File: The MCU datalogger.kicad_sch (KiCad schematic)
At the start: 0 parts

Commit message: Initial commit before syncing with GitHub
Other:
- company: (none) -> Precious Nedilyn B. Echapare
- title: (none) -> MCU Datalogger
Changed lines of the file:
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@@
 	(generator_version "9.0")
 	(paper "A4")
+	(title_block
+		(title "MCU Datalogger")
+		(rev "1")
+		(company "Precious Nedilyn B. Echapare")
+	)
 	(sheet_instances
 		(path "/"

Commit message: Have added required symbols to the schematic sheets.
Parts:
- added BT1: Battery, symbol Device:Battery
- added C1, C2, C3, C4: C, symbol Device:C
- added C5: C_Polarized, symbol Device:C_Polarized
- added D1, D2: LED, symbol Device:LED
- added R1, R2, R3, R4, R5, R6, R7: R, symbol Device:R
- added U1: ATMEGA328P-AU, ATMEGA328P-AU:QFP80P900X900X120-32N, symbol ATMEGA328P_AU:ATMEGA328P-AU
- added U2: DS1337S_, DS1337S_:SOIC127P600X175-8N, symbol DS1337S:DS1337S_
- added U3, U4: 24LC1025, symbol Memory_EEPROM:24LC1025
- added Y1, Y2: Crystal, symbol Device:Crystal
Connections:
- new net: U1.21 (GND), U1.3 (GND), U1.5 (GND)
- new net: U1.4 (VCC), U1.6 (VCC)
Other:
- added sheet Connectors (connectors.kicad_sch)

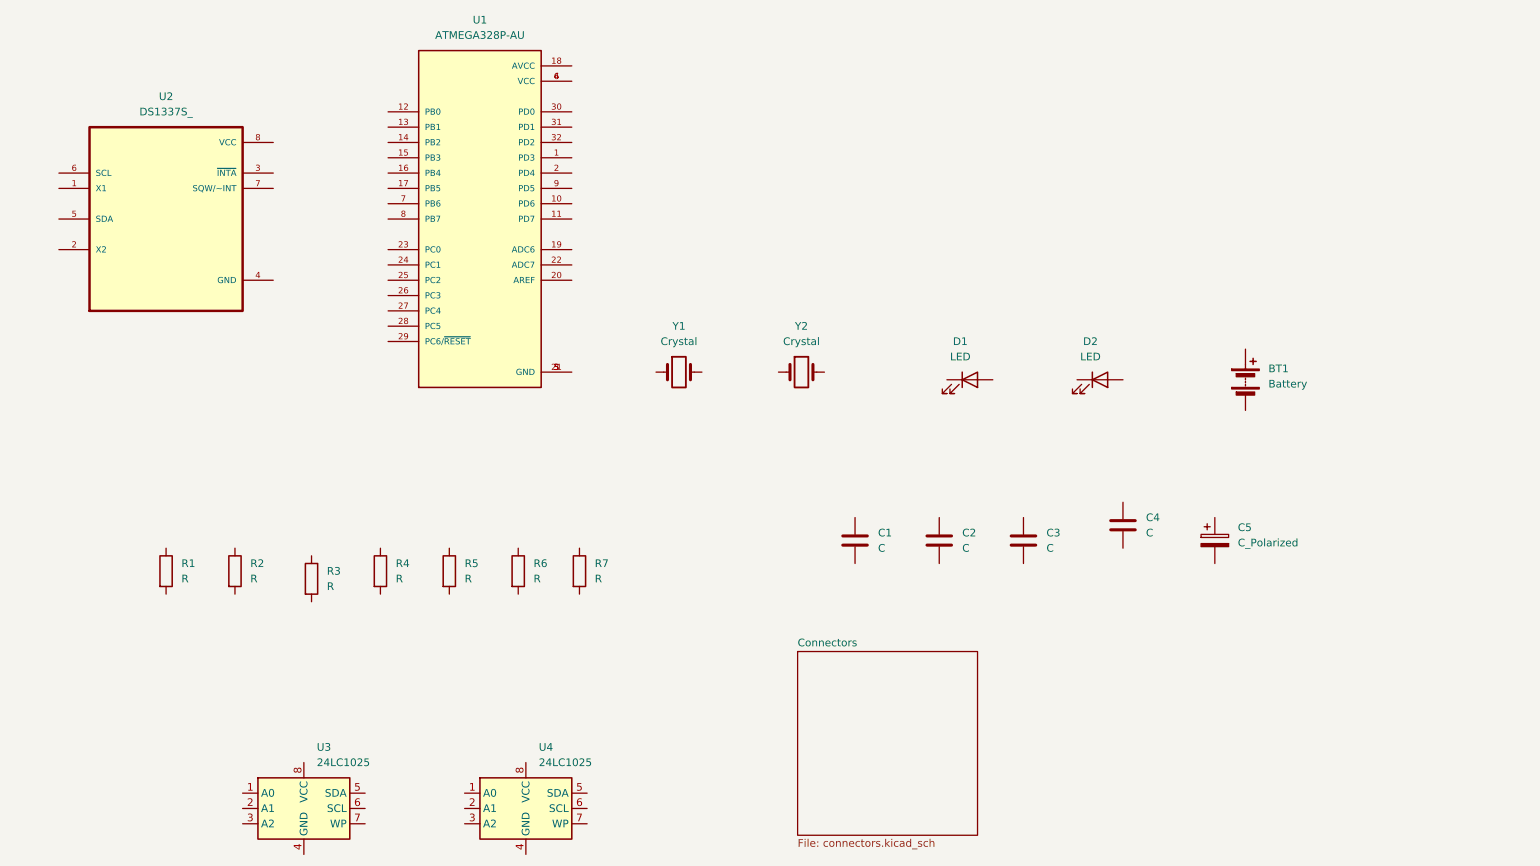
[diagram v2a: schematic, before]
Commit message: Added component values.
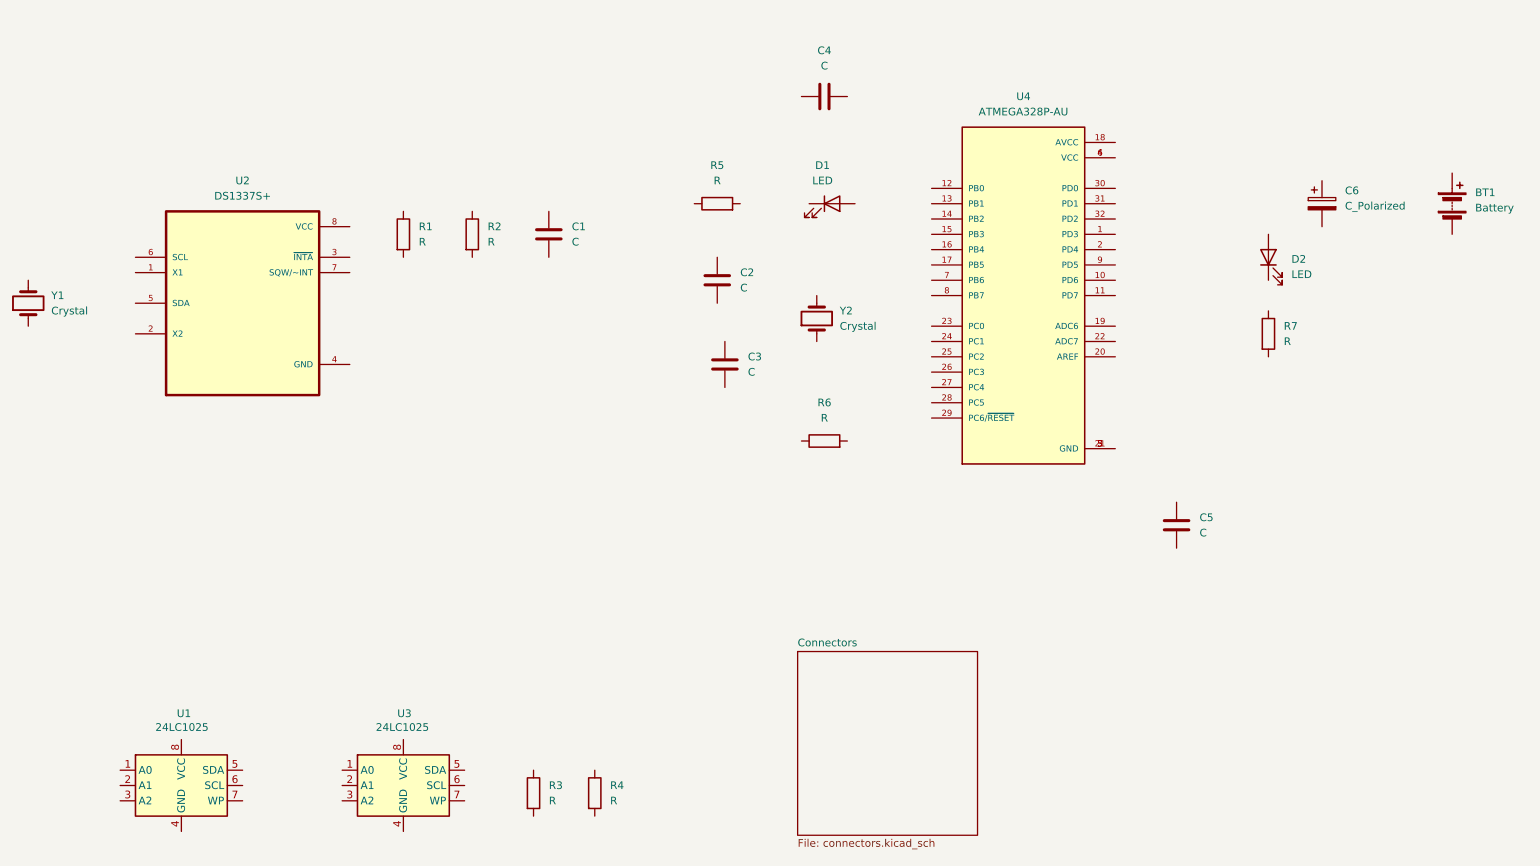
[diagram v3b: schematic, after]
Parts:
- added C1: C, symbol Device:C
- U2: value DS1337S_ -> DS1337S+
- renumbered C1 to C4, C4 to C5, C5 to C6, R4 to R1, R3 to R2, R2 to R3, R1 to R4, R6 to R5, R5 to R6, U3 to U1, U4 to U3, U1 to U4, Y2 to Y1, Y1 to Y2
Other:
- moved on the sheet: BT1, C2, C3, C4, C5, C6, D1, D2, R1, R2, R3, R4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

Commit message: Completed symbol-footprint associations.
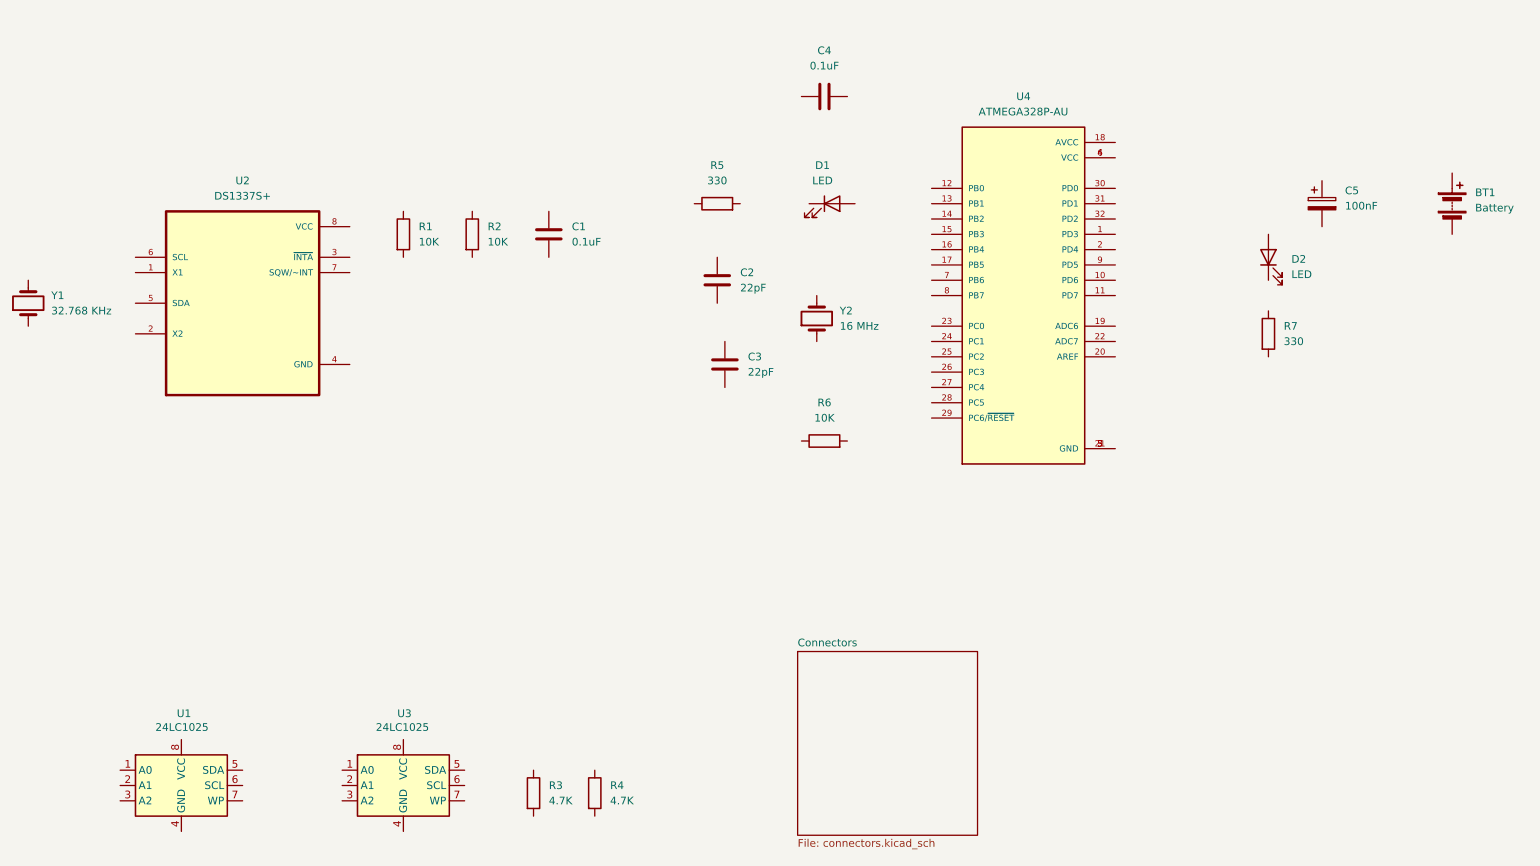
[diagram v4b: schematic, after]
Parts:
- removed C5: C, symbol Device:C
- BT1: footprint (none) -> Connector_PinHeader_2.54mm:PinHeader_1x02_P2.54mm_Vertical
- C1, C4: value C -> 0.1uF; footprint (none) -> Capacitor_SMD:C_0805_2012Metric
- C2, C3: value C -> 22pF; footprint (none) -> Capacitor_SMD:C_0805_2012Metric
- C5: renamed from C6; value C_Polarized -> 100nF; footprint (none) -> Capacitor_SMD:C_0805_2012Metric
- D1, D2: footprint (none) -> LED_SMD:LED_0805_2012Metric
- R1, R2, R6: value R -> 10K; footprint (none) -> Resistor_SMD:R_0805_2012Metric
- R3, R4: value R -> 4.7K; footprint (none) -> Resistor_SMD:R_0805_2012Metric
- R5, R7: value R -> 330; footprint (none) -> Resistor_SMD:R_0805_2012Metric
- U1, U3: footprint (none) -> Package_SO:SOIC-8-N7_3.9x4.9mm_P1.27mm
- Y1: value Crystal -> 32.768 KHz; footprint (none) -> Crystal:Crystal_SMD_5032-2Pin_5.0x3.2mm_HandSoldering
- Y2: value Crystal -> 16 MHz; footprint (none) -> Crystal:Crystal_SMD_5032-2Pin_5.0x3.2mm_HandSoldering
